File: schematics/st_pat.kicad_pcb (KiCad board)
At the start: 2 copper layers, 121.9 x 87 mm, 21 parts, among them J4 BATTERY, SW1 SW_PWR, SW2 BTN_RST, SW3 BTN, SW4 BTN, SW5 BTN, U1 GPS_Breakout_746, U2 FEATHER_M0_BASIC_PROTO, U3 LIS2MDL_ADAFRUIT, U4 Sharp_Display_4694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

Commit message: update schematics for new telemetry breakout board
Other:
- net class Default removed

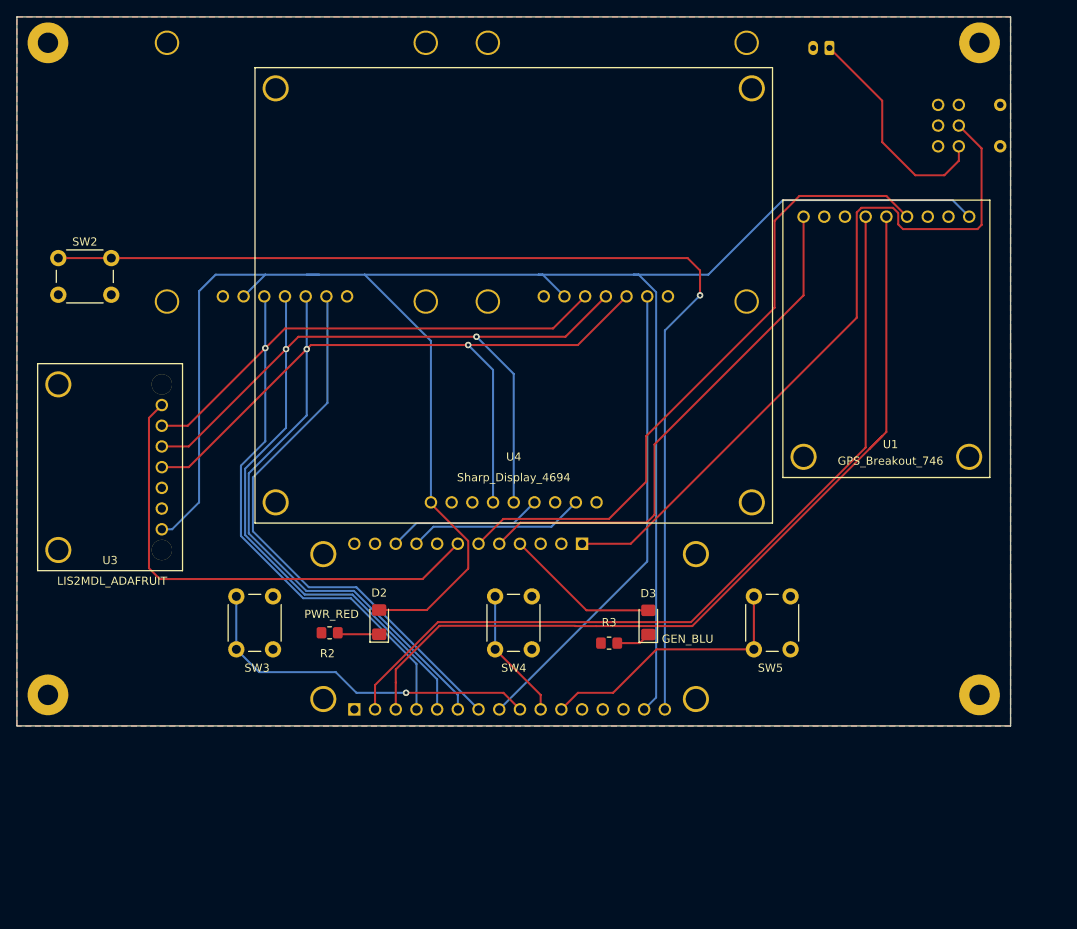
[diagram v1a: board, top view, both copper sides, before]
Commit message: fix sch review issues
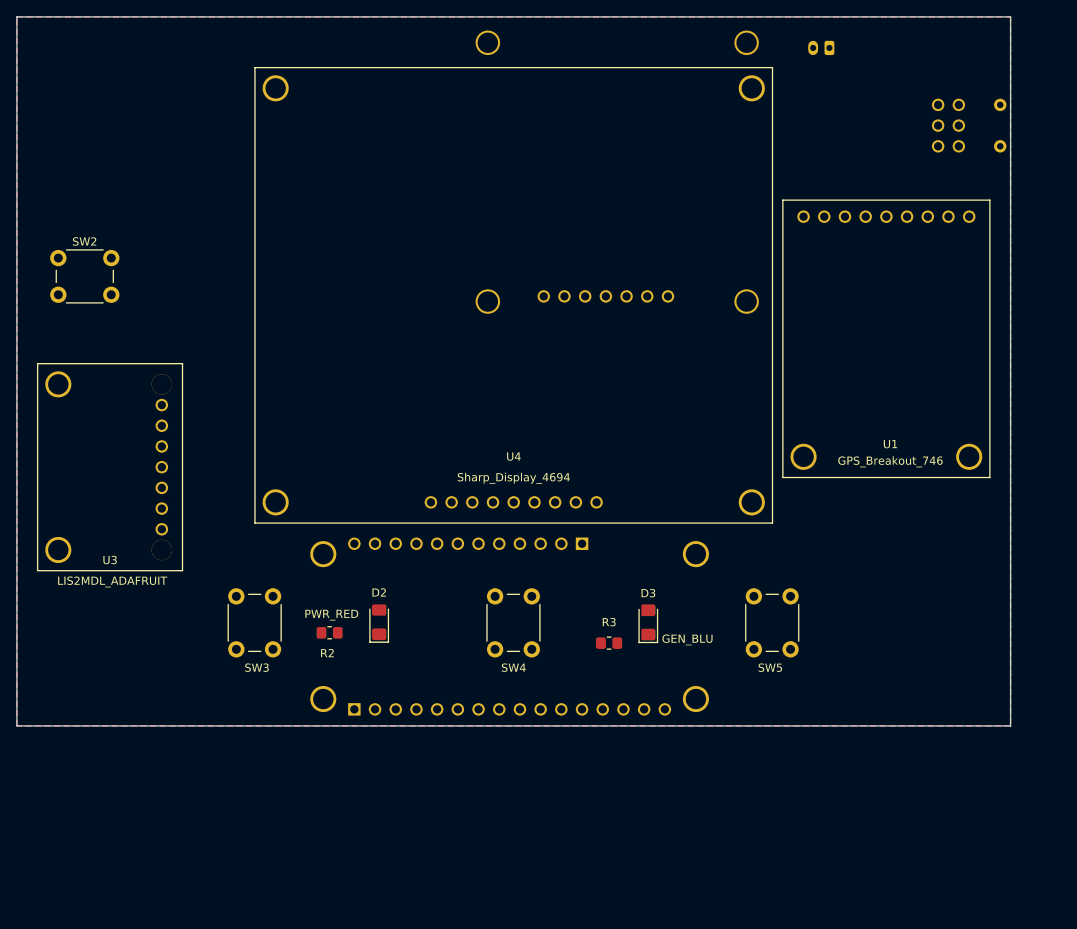
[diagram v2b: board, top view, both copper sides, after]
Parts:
- removed  : , MountingHole:MountingHole_2.5mm_Pad (x4)
- removed G***: LOGO, st_pat:Logo_SilkScreen_10mm
- removed U6: SRAD_GPS_RECEIVER, st_pat:Telemetry_Breakout
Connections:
- net /COTS_RECV_CS_A4 renamed /TELE_RTS_A4
- SW1 pad 1: (no net) -> unconnected-(SW1-Pad1)
- SW1 pad 2: (no net) -> unconnected-(SW1-Pad2)
- SW1 pad 3: (no net) -> unconnected-(SW1-Pad3)
- SW1 pad 4: (no net) -> unconnected-(SW1-Pad4)
- U1 pad 1: /GPS_PPS_D12 -> /GPS_PPS_D20
- U1 pad 2: (no net) -> unconnected-(U1-Pad2)
- U1 pad 6: /GPS_FIX_D11 -> /GPS_FIX_D21
- U1 pad 7: (no net) -> unconnected-(U1-Pad7)
- U1 pad 8: (no net) -> unconnected-(U1-Pad8)
- U2 pad P1_12: (no net) -> unconnected-(U2-PadP1_12)
- U2 pad P1_14: (no net) -> unconnected-(U2-PadP1_14)
- U2 pad P1_7: /SRAD_RECV_CS_A5 -> /TELE_CTS_A5
- U2 pad P2_11: (no net) -> /GPS_FIX_D21
- U2 pad P2_12: (no net) -> /GPS_PPS_D20
- U2 pad P2_2: (no net) -> unconnected-(U2-PadP2_2)
- U2 pad P2_3: (no net) -> unconnected-(U2-PadP2_3)
- U2 pad P2_5: /GPS_PPS_D12 -> /TELE_TX_D11
- U2 pad P2_6: /GPS_FIX_D11 -> /TELE_RX_D12
- U2 pad P2_8: (no net) -> unconnected-(U2-PadP2_8)
- U3 pad 2: (no net) -> unconnected-(U3-Pad2)
- U4 pad 2: (no net) -> unconnected-(U4-Pad2)
- U4 pad 7: (no net) -> unconnected-(U4-Pad7)
- U5 pad 1: (no net) -> /TELE_CTS_A5
- U5 pad 3: /SCK -> /TELE_RX_D12
- U5 pad 4: /MOSI -> /TELE_TX_D11
- U5 pad 5: /MISO -> +3V3
- U5 pad 6: +3V3 -> GND
- U5 pad 7: GND -> (no net)
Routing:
- net +3V3: track 251.2 -> 0.00 mm
- net /SCK: track 154.2 -> 0.00 mm, vias 2 -> 0
- net /MOSI: track 150.7 -> 0.00 mm, vias 2 -> 0
- net /RST: track 135.5 -> 0.00 mm, vias 1 -> 0
- net /MISO: track 123.0 -> 0.00 mm, vias 1 -> 0
- net /GPS_TX: track 105.8 -> 0.00 mm
- net /GPS_RX: track 103.6 -> 0.00 mm
- net +BATT: track 89.1 -> 0.00 mm
- net /GPS_FIX_D11: track 80.8 -> 0.00 mm
- net /SRAD_RECV_CS_A5: track 69.4 -> 0.00 mm
- net /GPS_PPS_D12: track 64.7 -> 0.00 mm
- net /CPS_CS_D10: track 60.9 -> 0.00 mm
- net /TELE_RTS_A4: track 58.2 -> 0.00 mm
- net /BTN_A3: track 44.6 -> 0.00 mm, vias 1 -> 0
- net /BTN_A1: track 33.2 -> 0.00 mm
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
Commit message: update telemetry breakout footprint and redo layout and routing
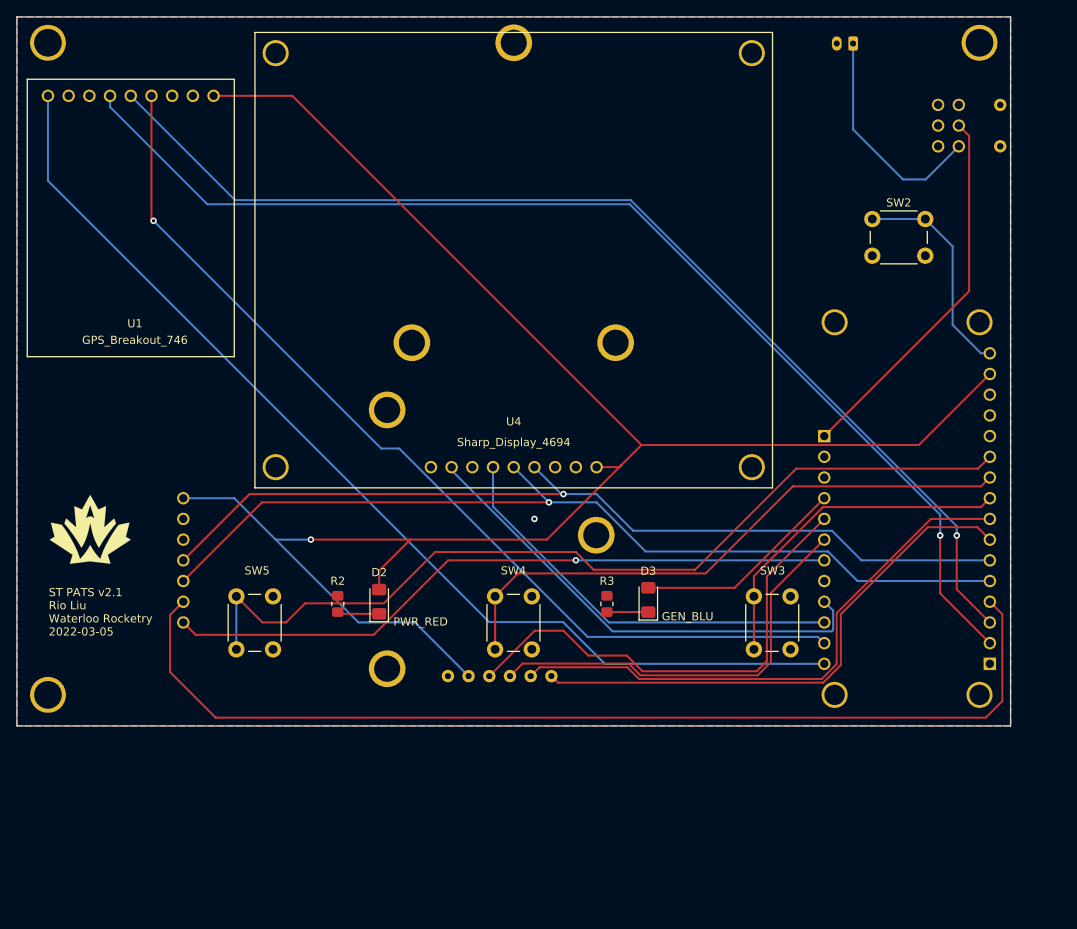
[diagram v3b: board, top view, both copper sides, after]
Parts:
- added G***: LOGO, Team_Logo:Logo_SilkScreen_10mm, F.Cu at (87.7, 100.3)
- added REF**: MountingHole_3mm_Pad, MountingHole:MountingHole_3mm_Pad, F.Cu at (196.8, 40.6)
- added REF**: MountingHole_3mm_Pad, MountingHole:MountingHole_3mm_Pad, F.Cu at (82.5, 120.7)
- added REF**: MountingHole_3mm_Pad, MountingHole:MountingHole_3mm_Pad, F.Cu at (82.5, 40.6)
- U3: moved to B.Cu
- moved SW2 100.0 mm to (183.7, 62.3)
- moved U1 93.9 mm to (92.7, 82.2)
- moved U2 50.9 mm to (188.0, 97.8), turned to -90 degrees
- moved U5 37.5 mm to (139.7, 40.6), turned to 180 degrees
- moved R3 4.82 mm to (151.1, 109.5), turned to 90 degrees
- moved U4 4.32 mm to (129.5, 92.7)
- moved R2 3.68 mm to (118.1, 109.5), turned to 90 degrees
- moved J4 2.96 mm to (181.3, 40.7)
- moved U3 2.93 mm to (81.4, 99.1), turned to -90 degrees
- moved D3 2.76 mm to (156.2, 109.0)
- moved D2 2.50 mm to (123.2, 109.2)
- renumbered SW5 to SW3, SW3 to SW5
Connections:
- SW3 pad 1: /BTN_A1 -> /BTN_A3
- SW5 pad 1: /BTN_A3 -> /BTN_A1
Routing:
- net +3V3: track 0.00 -> 221.2 mm, vias 0 -> 1
- net /GPS_RX: track 0.00 -> 142.2 mm, vias 0 -> 1
- net /GPS_TX: track 0.00 -> 136.7 mm, vias 0 -> 1
- net /GPS_PPS_D20: track 0.00 -> 130.2 mm
- net /MISO: track 0.00 -> 127.4 mm
- net /GPS_FIX_D21: track 0.00 -> 119.2 mm, vias 0 -> 1
- net /MOSI: track 0.00 -> 113.1 mm, vias 0 -> 1
- net /SCK: track 0.00 -> 110.6 mm, vias 0 -> 1
- net /BTN_A1: track 0.00 -> 110.5 mm
- net /CPS_CS_D10: track 0.00 -> 83.1 mm, vias 0 -> 1
- net /BTN_A2: track 0.00 -> 73.2 mm
- net /TELE_RTS_A4: track 0.00 -> 69.2 mm
- net /TELE_CTS_A5: track 0.00 -> 66.3 mm
- net /SHARP_DISP_D6: track 0.00 -> 59.4 mm
- net /TELE_TX_D11: track 0.00 -> 59.3 mm
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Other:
- board text added: "ST PATS v2.1 Rio Liu Waterloo Rocketry 2022-03-05"
- board text removed: "St Pats Rio Liu Waterloo Rocketry 2021-09-29"

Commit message: fix review issues
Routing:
- net /TELE_TX_D11: track 59.3 -> 61.3 mm
- net /TELE_RX_D12: track 51.7 -> 53.7 mm
- net /SHARP_DISP_D6: track 59.4 -> 60.0 mm
- net GND: vias 1 -> 0
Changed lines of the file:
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@@
     (effects (font (size 1 1) (thickness 0.15)) (justify left))
   )
-  (via (at 142.24 99.06) (size 0.8) (drill 0.4) (layers "F.Cu" "B.Cu") (free) (net 1))
   (segment (start 152.654 92.71) (end 152.908 92.456) (width 0.25) (layer "F.Cu") (net 2))
   (segment (start 149.86 92.71) (end 152.654 92.71) (width 0.25) (layer "F.Cu") (net 2))
@@
   (segment (start 177.8 111.76) (end 151.375386 111.76) (width 0.25) (layer "B.Cu") (net 12))
   (segment (start 137.16 97.544614) (end 137.16 92.71) (width 0.25) (layer "B.Cu") (net 12))
-  (segment (start 178.889511 112.702489) (end 178.742489 112.849511) (width 0.25) (layer "B.Cu") (net 13))
+  (segment (start 179.5 110.92) (end 179.5 112.25) (width 0.25) (layer "B.Cu") (net 13))
   (segment (start 132.08 93.100332) (end 132.08 92.71) (width 0.25) (layer "B.Cu") (net 13))
-  (segment (start 177.8 109.22) (end 178.889511 110.309511) (width 0.25) (layer "B.Cu") (net 13))
+  (segment (start 177.8 109.22) (end 179.5 110.92) (width 0.25) (layer "B.Cu") (net 13))
   (segment (start 151.829179 112.849511) (end 132.08 93.100332) (width 0.25) (layer "B.Cu") (net 13))
-  (segment (start 178.889511 110.309511) (end 178.889511 112.702489) (width 0.25) (layer "B.Cu") (net 13))
+  (segment (start 178.900489 112.849511) (end 179.5 112.25) (width 0.25) (layer "B.Cu") (net 13))
+  (segment (start 178.742489 112.849511) (end 178.900489 112.849511) (width 0.25) (layer "B.Cu") (net 13))
   (segment (start 178.742489 112.849511) (end 151.829179 112.849511) (width 0.25) (layer "B.Cu") (net 13))
   (segment (start 150.876 116.84) (end 145.752571 111.716571) (width 0.25) (layer "B.Cu") (net 14))
@@
   (segment (start 179.324 110.616282) (end 179.324 116.856802) (width 0.25) (layer "F.Cu") (net 30))
   (segment (start 148.844 115.824) (end 153.574 115.824) (width 0.25) (layer "F.Cu") (net 35))
+  (segment (start 155.5 117.75) (end 173 117.75) (width 0.25) (layer "F.Cu") (net 35))
+  (segment (start 173 117.75) (end 174.988511 115.761489) (width 0.25) (layer "F.Cu") (net 35))
+  (segment (start 145.796 112.776) (end 148.844 115.824) (width 0.25) (layer "F.Cu") (net 35))
   (segment (start 136.7 118.345) (end 142.269 112.776) (width 0.25) (layer "F.Cu") (net 35))
+  (segment (start 174.988511 101.871489) (end 177.8 99.06) (width 0.25) (layer "F.Cu") (net 35))
+  (segment (start 142.269 112.776) (end 145.796 112.776) (width 0.25) (layer "F.Cu") (net 35))
+  (segment (start 174.988511 115.761489) (end 174.988511 101.871489) (width 0.25) (layer "F.Cu") (net 35))
   (segment (start 153.574 115.824) (end 155.5 117.75) (width 0.25) (layer "F.Cu") (net 35))
-  (segment (start 170.75 116.5) (end 170.75 106.11) (width 0.25) (layer "F.Cu") (net 35))
-  (segment (start 170.75 106.11) (end 177.8 99.06) (width 0.25) (layer "F.Cu") (net 35))
-  (segment (start 169.5 117.75) (end 170.75 116.5) (width 0.25) (layer "F.Cu") (net 35))
-  (segment (start 145.796 112.776) (end 148.844 115.824) (width 0.25) (layer "F.Cu") (net 35))
-  (segment (start 155.5 117.75) (end 169.5 117.75) (width 0.25) (layer "F.Cu") (net 35))
-  (segment (start 142.269 112.776) (end 145.796 112.776) (width 0.25) (layer "F.Cu") (net 35))
-  (segment (start 169.635718 118.25) (end 171.25 116.635718) (width 0.25) (layer "F.Cu") (net 36))
+  (segment (start 175.5 103.9) (end 177.8 101.6) (width 0.25) (layer "F.Cu") (net 36))
+  (segment (start 140.776031 116.808969) (end 153.808969 116.808969) (width 0.25) (layer "F.Cu") (net 36))
+  (segment (start 155.25 118.25) (end 173.135717 118.25) (width 0.25) (layer "F.Cu") (net 36))
+  (segment (start 153.808969 116.808969) (end 155.25 118.25) (width 0.25) (layer "F.Cu") (net 36))
+  (segment (start 173.135717 118.25) (end 175.5 115.885717) (width 0.25) (layer "F.Cu") (net 36))
   (segment (start 139.24 118.345) (end 140.776031 116.808969) (width 0.25) (layer "F.Cu") (net 36))
-  (segment (start 140.776031 116.808969) (end 153.808969 116.808969) (width 0.25) (layer "F.Cu") (net 36))
-  (segment (start 155.25 118.25) (end 169.635718 118.25) (width 0.25) (layer "F.Cu") (net 36))
-  (segment (start 153.808969 116.808969) (end 155.25 118.25) (width 0.25) (layer "F.Cu") (net 36))
-  (segment (start 171.25 116.635718) (end 171.25 108.15) (width 0.25) (layer "F.Cu") (net 36))
-  (segment (start 171.25 108.15) (end 177.8 101.6) (width 0.25) (layer "F.Cu") (net 36))
+  (segment (start 175.5 115.885717) (end 175.5 103.9) (width 0.25) (layer "F.Cu") (net 36))
   (zone (net 1) (net_name "GND") (layer "F.Cu") (hatch edge 0.508)
     (connect_pads (clearance 0.508))

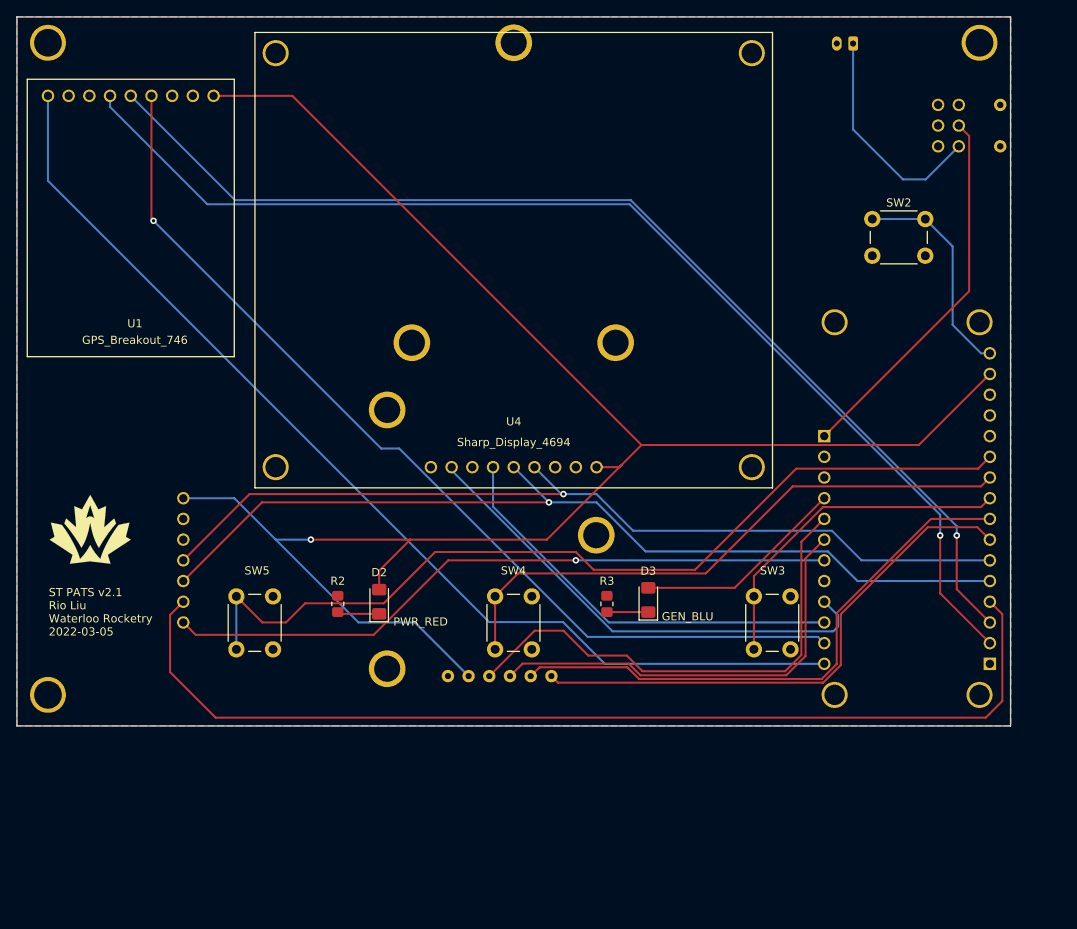
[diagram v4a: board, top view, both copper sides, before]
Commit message: add dimensions to board
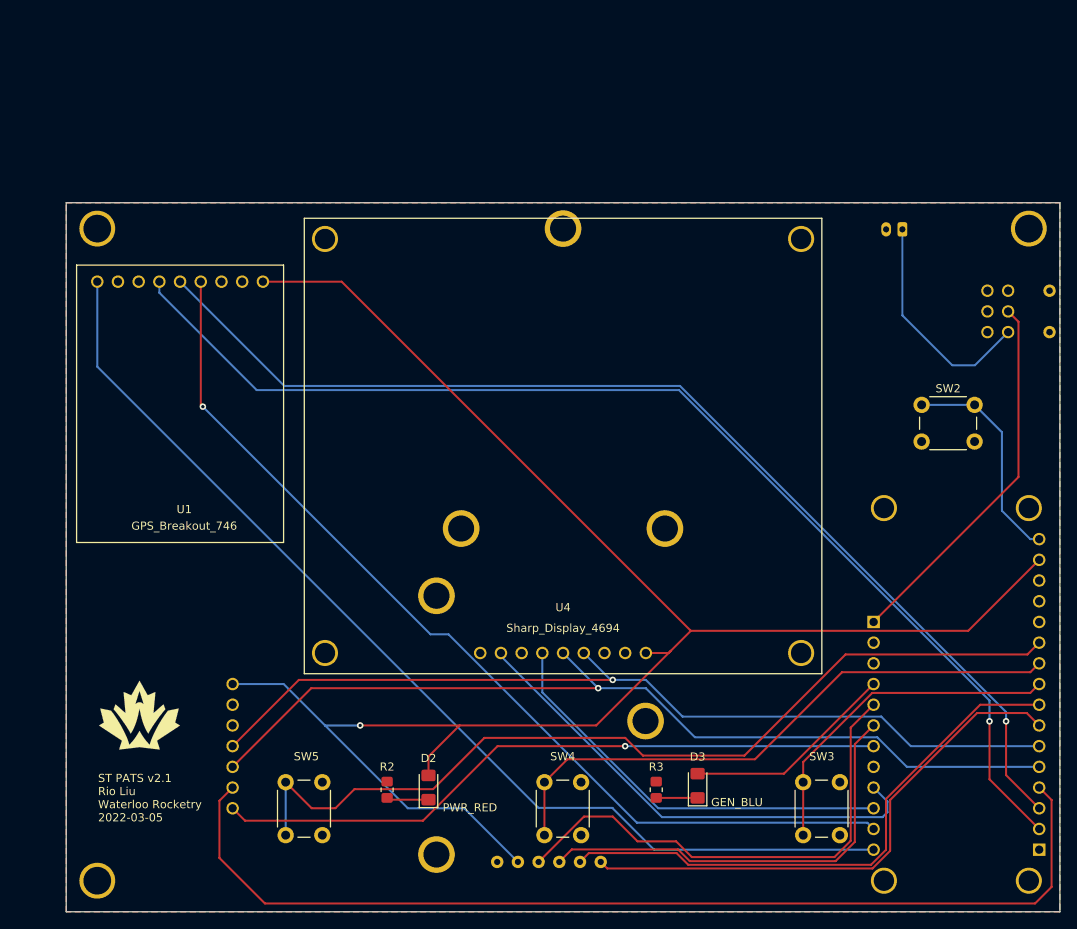
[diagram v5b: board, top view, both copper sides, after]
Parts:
- moved D2 23.6 mm to (129.2, 132.0)
- moved U1 23.6 mm to (98.8, 105.0)
- moved U4 23.6 mm to (135.6, 115.5)
- moved D3 23.6 mm to (162.3, 131.8)
- moved G*** 23.6 mm to (93.8, 123.1)
- moved R3 23.6 mm to (157.2, 132.3)
- moved REF** 23.6 mm to (202.9, 63.4)
- moved SW2 23.6 mm to (189.7, 85.1)
- moved SW3 23.6 mm to (175.2, 137.9)
- moved SW4 23.6 mm to (143.5, 137.9)
- moved U5 23.6 mm to (145.8, 63.4)
- moved J4 23.6 mm to (187.4, 63.5)
- moved SW1 23.6 mm to (197.8, 71.1)
- moved R2 23.6 mm to (124.2, 132.3)
- moved REF** 23.6 mm to (88.6, 63.4)
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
